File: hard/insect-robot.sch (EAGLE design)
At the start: 4 parts, among them SW1 MK-12C02, U1 ATMEGA328P-QFN32

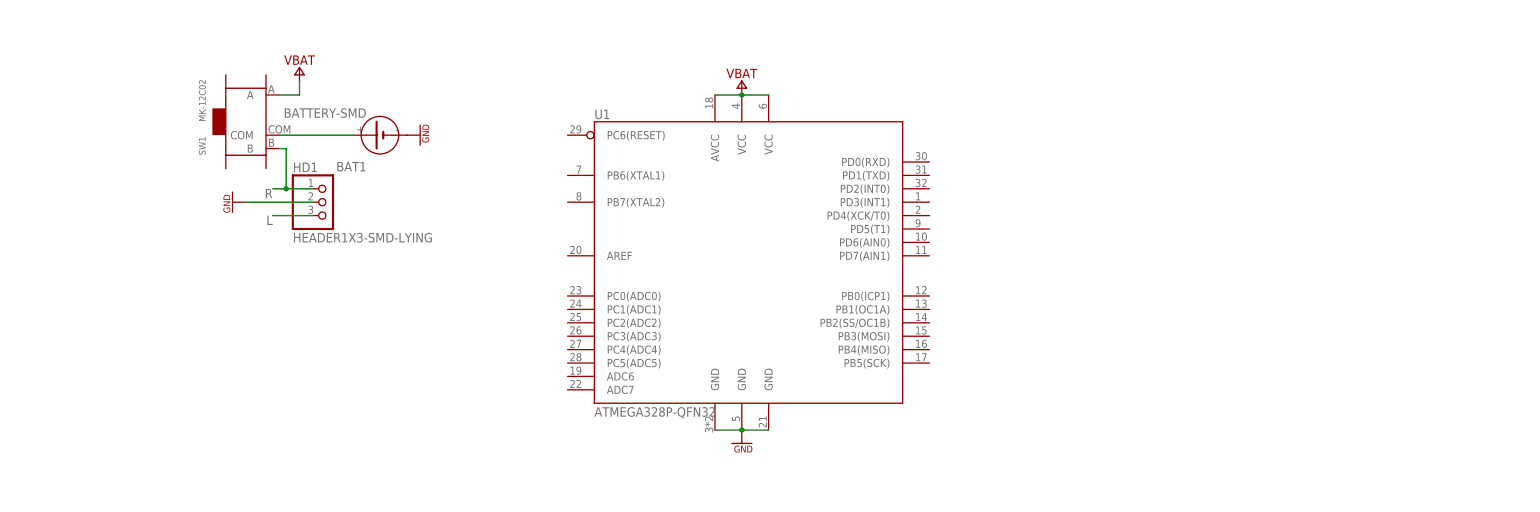
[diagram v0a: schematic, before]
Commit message: Add bluetooth module
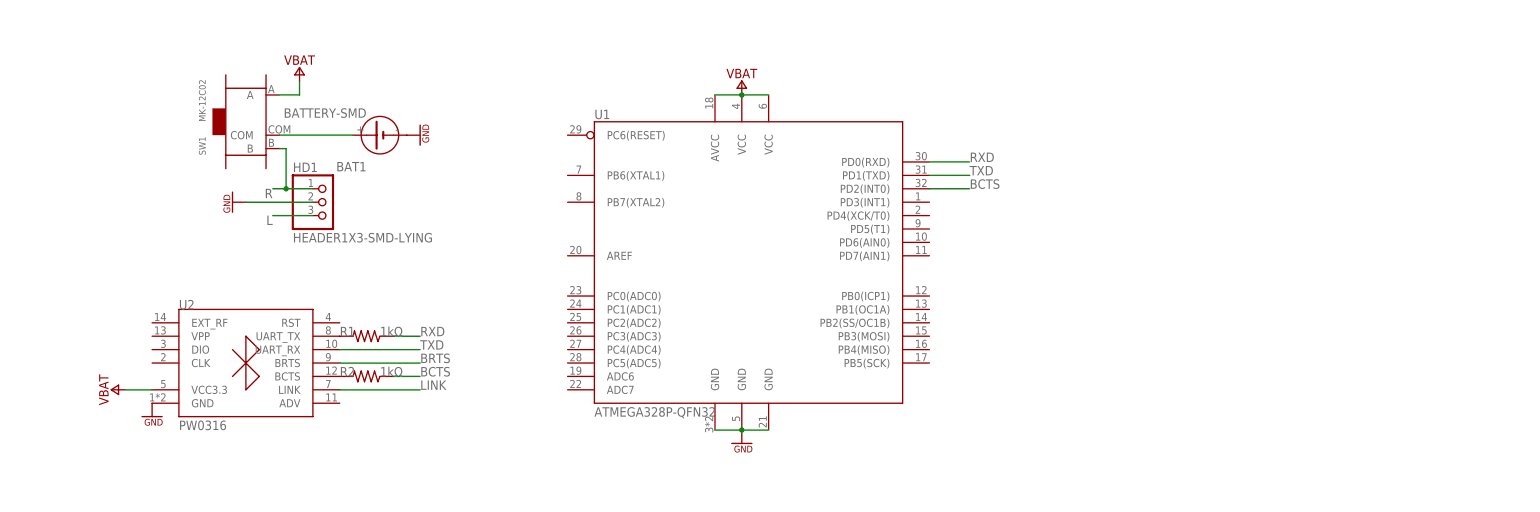
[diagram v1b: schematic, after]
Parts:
- added R1, R2: 1kΩ, MyLibrary:RES-0603
- added U2: PW0316, MyLibrary:PW0316
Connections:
- new net BCTS: R2.1, U1.PD2(INT0)
- new net BRTS: U2.BRTS
- new net LINK: U2.LINK
- new net R-BCTS: R2.2, U2.BCTS
- new net R-TX: R1.2, U2.UART_TX
- new net RXD: R1.1, U1.PD0(RXD)
- new net TXD: U1.PD1(TXD), U2.UART_RX
- net GND: now also U2.GND
- net VBAT: now also U2.VCC3.3
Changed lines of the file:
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@@
 <part name="HD1" library="MyLibrary" deviceset="HEADER1X3" device="-SMD-LYING"/>
 <part name="SUPPLY5" library="MyLibrary" deviceset="GND" device=""/>
+<part name="U2" library="MyLibrary" deviceset="PW0316" device=""/>
+<part name="SUPPLY6" library="MyLibrary" deviceset="VBAT" device=""/>
+<part name="SUPPLY7" library="MyLibrary" deviceset="GND" device=""/>
+<part name="R1" library="MyLibrary" deviceset="RES" device="-0603" value="1kΩ"/>
+<part name="R2" library="MyLibrary" deviceset="RES" device="-0603" value="1kΩ"/>
 </parts>
 <sheets>
@@
 <instance part="HD1" gate="A" x="-78.74" y="12.7"/>
 <instance part="SUPPLY5" gate="GND" x="-96.52" y="12.7" rot="R270"/>
+<instance part="U2" gate="P" x="-93.98" y="-17.78"/>
+<instance part="SUPPLY6" gate="VBAT" x="-119.38" y="-22.86" rot="R90"/>
+<instance part="SUPPLY7" gate="GND" x="-111.76" y="-27.94"/>
+<instance part="R1" gate="A" x="-71.12" y="-12.7" smashed="yes">
+<attribute name="NAME" x="-76.2" y="-12.7" size="1.778" layer="95"/>
+<attribute name="VALUE" x="-68.58" y="-12.7" size="1.778" layer="96"/>
+</instance>
+<instance part="R2" gate="A" x="-71.12" y="-20.32" smashed="yes">
+<attribute name="NAME" x="-76.2" y="-20.32" size="1.778" layer="95"/>
+<attribute name="VALUE" x="-68.58" y="-20.32" size="1.778" layer="96"/>
+</instance>
 </instances>
 <busses>
@@
 <wire x1="-83.82" y1="33.02" x2="-87.63" y2="33.02" width="0.1524" layer="91"/>
 </segment>
+<segment>
+<pinref part="U2" gate="P" pin="VCC3.3"/>
+<pinref part="SUPPLY6" gate="VBAT" pin="VBAT"/>
+<wire x1="-111.76" y1="-22.86" x2="-116.84" y2="-22.86" width="0.1524" layer="91"/>
+</segment>
 </net>
 <net name="GND" class="0">
@@
 <wire x1="-81.28" y1="12.7" x2="-93.98" y2="12.7" width="0.1524" layer="91"/>
 <pinref part="SUPPLY5" gate="GND" pin="GND"/>
+</segment>
+<segment>
+<pinref part="U2" gate="P" pin="GND"/>
+<pinref part="SUPPLY7" gate="GND" pin="GND"/>
 </segment>
 </net>
@@
 </segment>
 </net>
+<net name="RXD" class="0">
+<segment>
+<pinref part="U1" gate="P" pin="PD0(RXD)"/>
+<wire x1="35.56" y1="20.32" x2="43.18" y2="20.32" width="0.1524" layer="91"/>
+<label x="43.18" y="20.32" size="1.778" layer="95" font="vector"/>
+</segment>
+<segment>
+<pinref part="R1" gate="A" pin="1"/>
+<wire x1="-66.04" y1="-12.7" x2="-60.96" y2="-12.7" width="0.1524" layer="91"/>
+<label x="-60.96" y="-12.7" size="1.778" layer="95" font="vector"/>
+</segment>
+</net>
+<net name="TXD" class="0">
+<segment>
+<pinref part="U1" gate="P" pin="PD1(TXD)"/>
+<wire x1="35.56" y1="17.78" x2="43.18" y2="17.78" width="0.1524" layer="91"/>
+<label x="43.18" y="17.78" size="1.778" layer="95" font="vector"/>
+</segment>
+<segment>
+<pinref part="U2" gate="P" pin="UART_RX"/>
+<wire x1="-76.2" y1="-15.24" x2="-60.96" y2="-15.24" width="0.1524" layer="91"/>
+<label x="-60.96" y="-15.24" size="1.778" layer="95" font="vector"/>
+</segment>
+</net>
+<net name="BRTS" class="0">
+<segment>
+<pinref part="U2" gate="P" pin="BRTS"/>
+<wire x1="-76.2" y1="-17.78" x2="-60.96" y2="-17.78" width="0.1524" layer="91"/>
+<label x="-60.96" y="-17.78" size="1.778" layer="95" font="vector"/>
+</segment>
+</net>
+<net name="R-BCTS" class="0">
+<segment>
+<pinref part="U2" gate="P" pin="BCTS"/>
+<pinref part="R2" gate="A" pin="2"/>
+</segment>
+</net>
+<net name="BCTS" class="0">
+<segment>
+<pinref part="R2" gate="A" pin="1"/>
+<wire x1="-66.04" y1="-20.32" x2="-60.96" y2="-20.32" width="0.1524" layer="91"/>
+<label x="-60.96" y="-20.32" size="1.778" layer="95" font="vector"/>
+</segment>
+<segment>
+<pinref part="U1" gate="P" pin="PD2(INT0)"/>
+<wire x1="35.56" y1="15.24" x2="43.18" y2="15.24" width="0.1524" layer="91"/>
+<label x="43.18" y="15.24" size="1.778" layer="95" font="vector"/>
+</segment>
+</net>
+<net name="R-TX" class="0">
+<segment>
+<pinref part="U2" gate="P" pin="UART_TX"/>
+<pinref part="R1" gate="A" pin="2"/>
+</segment>
+</net>
+<net name="LINK" class="0">
+<segment>
+<pinref part="U2" gate="P" pin="LINK"/>
+<wire x1="-76.2" y1="-22.86" x2="-60.96" y2="-22.86" width="0.1524" layer="91"/>
+<label x="-60.96" y="-22.86" size="1.778" layer="95" font="vector"/>
+</segment>
+</net>

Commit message: Add MOSFET for charging control
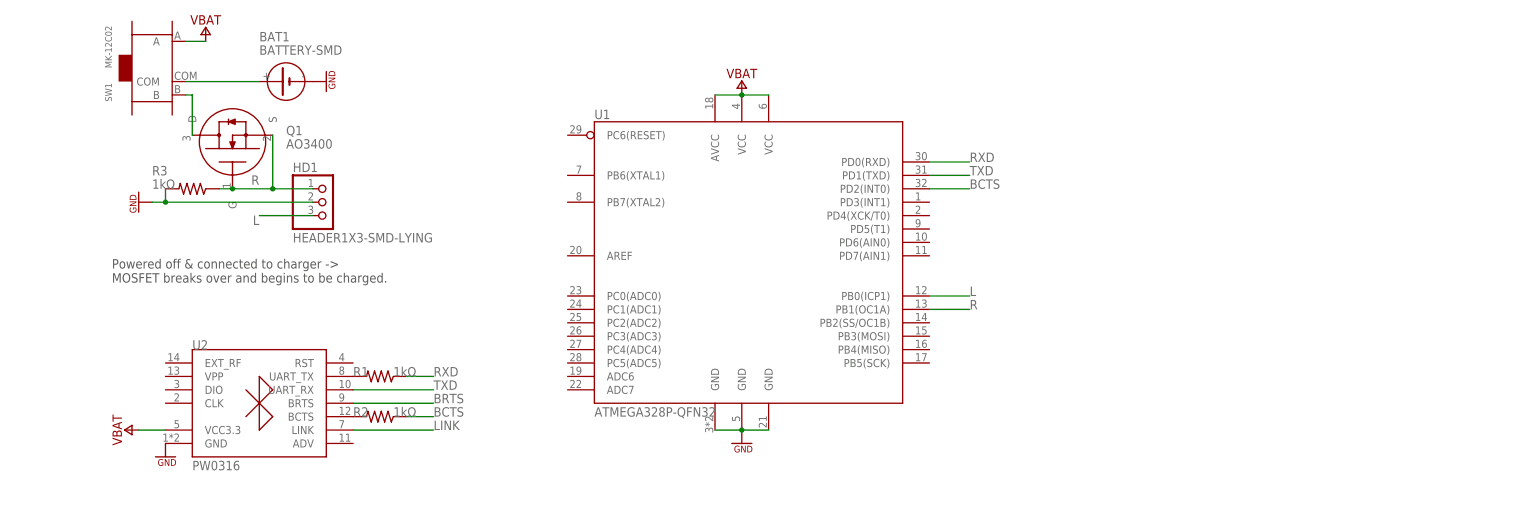
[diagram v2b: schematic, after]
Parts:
- added Q1: AO3400, MyLibrary:MOSFET-SOT23
- added R3: 1kΩ, MyLibrary:RES-0603
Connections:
- new net N$1: Q1.D, SW1.B
- net GND: now also R3.2
- net L: now also U1.PB0(ICP1)
- net R: now also Q1.G, Q1.S, R3.1, U1.PB1(OC1A); no longer SW1.B
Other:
- note added: "Powered off & connected to charger -> MOSFET breaks over and begins to be charged."
- moved on the sheet: BAT1, R1, R2, SW1, U2
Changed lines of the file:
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@@
 <part name="R1" library="MyLibrary" deviceset="RES" device="-0603" value="1kΩ"/>
 <part name="R2" library="MyLibrary" deviceset="RES" device="-0603" value="1kΩ"/>
+<part name="Q1" library="MyLibrary" deviceset="MOSFET" device="-SOT23" value="AO3400"/>
+<part name="R3" library="MyLibrary" deviceset="RES" device="-0603" value="1kΩ"/>
 </parts>
 <sheets>
 <sheet>
 <plain>
+<text x="-119.38" y="-2.54" size="1.778" layer="97">Powered off &amp; connected to charger -&gt;
+MOSFET breaks over and begins to be charged.</text>
 </plain>
 <instances>
@@
 <instance part="SUPPLY1" gate="VBAT" x="0" y="35.56"/>
 <instance part="SUPPLY2" gate="GND" x="0" y="-33.02"/>
-<instance part="SW1" gate="G$1" x="-93.98" y="27.94"/>
-<instance part="BAT1" gate="A" x="-68.58" y="25.4" rot="R180"/>
-<instance part="SUPPLY3" gate="VBAT" x="-83.82" y="38.1"/>
-<instance part="SUPPLY4" gate="GND" x="-60.96" y="25.4" rot="R90"/>
+<instance part="SW1" gate="G$1" x="-111.76" y="38.1"/>
+<instance part="BAT1" gate="A" x="-86.36" y="35.56" smashed="yes" rot="R180">
+<attribute name="NAME" x="-91.44" y="43.18" size="1.778" layer="95"/>
+<attribute name="VALUE" x="-91.44" y="40.64" size="1.778" layer="96"/>
+</instance>
+<instance part="SUPPLY3" gate="VBAT" x="-101.6" y="45.72"/>
+<instance part="SUPPLY4" gate="GND" x="-78.74" y="35.56" rot="R90"/>
 <instance part="HD1" gate="A" x="-78.74" y="12.7"/>
-<instance part="SUPPLY5" gate="GND" x="-96.52" y="12.7" rot="R270"/>
-<instance part="U2" gate="P" x="-93.98" y="-17.78"/>
-<instance part="SUPPLY6" gate="VBAT" x="-119.38" y="-22.86" rot="R90"/>
-<instance part="SUPPLY7" gate="GND" x="-111.76" y="-27.94"/>
-<instance part="R1" gate="A" x="-71.12" y="-12.7" smashed="yes">
-<attribute name="NAME" x="-76.2" y="-12.7" size="1.778" layer="95"/>
-<attribute name="VALUE" x="-68.58" y="-12.7" size="1.778" layer="96"/>
-</instance>
-<instance part="R2" gate="A" x="-71.12" y="-20.32" smashed="yes">
-<attribute name="NAME" x="-76.2" y="-20.32" size="1.778" layer="95"/>
-<attribute name="VALUE" x="-68.58" y="-20.32" size="1.778" layer="96"/>
+<instance part="SUPPLY5" gate="GND" x="-114.3" y="12.7" rot="R270"/>
+<instance part="U2" gate="P" x="-91.44" y="-25.4"/>
+<instance part="SUPPLY6" gate="VBAT" x="-116.84" y="-30.48" rot="R90"/>
+<instance part="SUPPLY7" gate="GND" x="-109.22" y="-35.56"/>
+<instance part="R1" gate="A" x="-68.58" y="-20.32" smashed="yes">
+<attribute name="NAME" x="-73.66" y="-20.32" size="1.778" layer="95"/>
+<attribute name="VALUE" x="-66.04" y="-20.32" size="1.778" layer="96"/>
+</instance>
+<instance part="R2" gate="A" x="-68.58" y="-27.94" smashed="yes">
+<attribute name="NAME" x="-73.66" y="-27.94" size="1.778" layer="95"/>
+<attribute name="VALUE" x="-66.04" y="-27.94" size="1.778" layer="96"/>
+</instance>
+<instance part="Q1" gate="A" x="-96.52" y="22.86" smashed="yes" rot="R90">
+<attribute name="NAME" x="-86.36" y="25.4" size="1.778" layer="95"/>
+<attribute name="VALUE" x="-86.36" y="22.86" size="1.778" layer="96"/>
+</instance>
+<instance part="R3" gate="A" x="-104.14" y="15.24" smashed="yes">
+<attribute name="NAME" x="-111.76" y="17.78" size="1.778" layer="95"/>
+<attribute name="VALUE" x="-111.76" y="15.24" size="1.778" layer="96"/>
 </instance>
 </instances>
@@
 </segment>
 <segment>
-<pinref part="SUPPLY3" gate="VBAT" pin="VBAT"/>
-<wire x1="-83.82" y1="35.56" x2="-83.82" y2="33.02" width="0.1524" layer="91"/>
-<pinref part="SW1" gate="G$1" pin="A"/>
-<wire x1="-83.82" y1="33.02" x2="-87.63" y2="33.02" width="0.1524" layer="91"/>
-</segment>
-<segment>
 <pinref part="U2" gate="P" pin="VCC3.3"/>
 <pinref part="SUPPLY6" gate="VBAT" pin="VBAT"/>
-<wire x1="-111.76" y1="-22.86" x2="-116.84" y2="-22.86" width="0.1524" layer="91"/>
+<wire x1="-109.22" y1="-30.48" x2="-114.3" y2="-30.48" width="0.1524" layer="91"/>
+</segment>
+<segment>
+<pinref part="SUPPLY3" gate="VBAT" pin="VBAT"/>
+<pinref part="SW1" gate="G$1" pin="A"/>
+<wire x1="-101.6" y1="43.18" x2="-105.41" y2="43.18" width="0.1524" layer="91"/>
 </segment>
 </net>
@@
 <segment>
 <pinref part="HD1" gate="A" pin="2"/>
-<wire x1="-81.28" y1="12.7" x2="-93.98" y2="12.7" width="0.1524" layer="91"/>
+<wire x1="-81.28" y1="12.7" x2="-109.22" y2="12.7" width="0.1524" layer="91"/>
 <pinref part="SUPPLY5" gate="GND" pin="GND"/>
+<pinref part="R3" gate="A" pin="2"/>
+<wire x1="-109.22" y1="12.7" x2="-111.76" y2="12.7" width="0.1524" layer="91"/>
+<wire x1="-109.22" y1="15.24" x2="-109.22" y2="12.7" width="0.1524" layer="91"/>
+<junction x="-109.22" y="12.7"/>
 </segment>
 <segment>
@@
 <pinref part="BAT1" gate="A" pin="+"/>
 <pinref part="SW1" gate="G$1" pin="COM"/>
-<wire x1="-73.66" y1="25.4" x2="-87.63" y2="25.4" width="0.1524" layer="91"/>
+<wire x1="-91.44" y1="35.56" x2="-105.41" y2="35.56" width="0.1524" layer="91"/>
 </segment>
 </net>
@@
 <segment>
 <pinref part="HD1" gate="A" pin="1"/>
-<wire x1="-81.28" y1="15.24" x2="-86.36" y2="15.24" width="0.1524" layer="91"/>
-<wire x1="-86.36" y1="15.24" x2="-86.36" y2="22.86" width="0.1524" layer="91"/>
-<pinref part="SW1" gate="G$1" pin="B"/>
-<wire x1="-86.36" y1="22.86" x2="-87.63" y2="22.86" width="0.1524" layer="91"/>
-<wire x1="-86.36" y1="15.24" x2="-88.9" y2="15.24" width="0.1524" layer="91"/>
-<junction x="-86.36" y="15.24"/>
-<label x="-88.9" y="15.24" size="1.778" layer="95" font="vector" rot="R180"/>
+<wire x1="-81.28" y1="15.24" x2="-88.9" y2="15.24" width="0.1524" layer="91"/>
+<label x="-91.44" y="17.78" size="1.778" layer="95" font="vector" rot="R180"/>
+<pinref part="Q1" gate="A" pin="G"/>
+<wire x1="-88.9" y1="15.24" x2="-96.52" y2="15.24" width="0.1524" layer="91"/>
+<pinref part="Q1" gate="A" pin="S"/>
+<wire x1="-88.9" y1="25.4" x2="-88.9" y2="15.24" width="0.1524" layer="91"/>
+<junction x="-88.9" y="15.24"/>
+<pinref part="R3" gate="A" pin="1"/>
+<wire x1="-96.52" y1="15.24" x2="-99.06" y2="15.24" width="0.1524" layer="91"/>
+<junction x="-96.52" y="15.24"/>
+</segment>
+<segment>
+<pinref part="U1" gate="P" pin="PB1(OC1A)"/>
+<wire x1="35.56" y1="-7.62" x2="43.18" y2="-7.62" width="0.1524" layer="91"/>
+<label x="43.18" y="-7.62" size="1.778" layer="95" font="vector"/>
 </segment>
 </net>
@@
 <segment>
 <pinref part="HD1" gate="A" pin="3"/>
-<wire x1="-81.28" y1="10.16" x2="-88.9" y2="10.16" width="0.1524" layer="91"/>
-<label x="-88.9" y="10.16" size="1.778" layer="95" font="vector" rot="R180"/>
+<wire x1="-81.28" y1="10.16" x2="-91.44" y2="10.16" width="0.1524" layer="91"/>
+<label x="-91.44" y="10.16" size="1.778" layer="95" font="vector" rot="R180"/>
+</segment>
+<segment>
+<pinref part="U1" gate="P" pin="PB0(ICP1)"/>
+<wire x1="35.56" y1="-5.08" x2="43.18" y2="-5.08" width="0.1524" layer="91"/>
+<label x="43.18" y="-5.08" size="1.778" layer="95" font="vector"/>
 </segment>
 </net>
@@
 <segment>
 <pinref part="R1" gate="A" pin="1"/>
-<wire x1="-66.04" y1="-12.7" x2="-60.96" y2="-12.7" width="0.1524" layer="91"/>
-<label x="-60.96" y="-12.7" size="1.778" layer="95" font="vector"/>
+<wire x1="-63.5" y1="-20.32" x2="-58.42" y2="-20.32" width="0.1524" layer="91"/>
+<label x="-58.42" y="-20.32" size="1.778" layer="95" font="vector"/>
 </segment>
 </net>
@@
 <segment>
 <pinref part="U2" gate="P" pin="UART_RX"/>
-<wire x1="-76.2" y1="-15.24" x2="-60.96" y2="-15.24" width="0.1524" layer="91"/>
-<label x="-60.96" y="-15.24" size="1.778" layer="95" font="vector"/>
+<wire x1="-73.66" y1="-22.86" x2="-58.42" y2="-22.86" width="0.1524" layer="91"/>
+<label x="-58.42" y="-22.86" size="1.778" layer="95" font="vector"/>
 </segment>
 </net>
@@
 <segment>
 <pinref part="U2" gate="P" pin="BRTS"/>
-<wire x1="-76.2" y1="-17.78" x2="-60.96" y2="-17.78" width="0.1524" layer="91"/>
-<label x="-60.96" y="-17.78" size="1.778" layer="95" font="vector"/>
+<wire x1="-73.66" y1="-25.4" x2="-58.42" y2="-25.4" width="0.1524" layer="91"/>
+<label x="-58.42" y="-25.4" size="1.778" layer="95" font="vector"/>
 </segment>
 </net>
@@
 <segment>
 <pinref part="R2" gate="A" pin="1"/>
-<wire x1="-66.04" y1="-20.32" x2="-60.96" y2="-20.32" width="0.1524" layer="91"/>
-<label x="-60.96" y="-20.32" size="1.778" layer="95" font="vector"/>
+<wire x1="-63.5" y1="-27.94" x2="-58.42" y2="-27.94" width="0.1524" layer="91"/>
+<label x="-58.42" y="-27.94" size="1.778" layer="95" font="vector"/>
 </segment>
 <segment>
@@
 <segment>
 <pinref part="U2" gate="P" pin="LINK"/>
-<wire x1="-76.2" y1="-22.86" x2="-60.96" y2="-22.86" width="0.1524" layer="91"/>
-<label x="-60.96" y="-22.86" size="1.778" layer="95" font="vector"/>
+<wire x1="-73.66" y1="-30.48" x2="-58.42" y2="-30.48" width="0.1524" layer="91"/>
+<label x="-58.42" y="-30.48" size="1.778" layer="95" font="vector"/>
+</segment>
+</net>
+<net name="N$1" class="0">
+<segment>
+<pinref part="Q1" gate="A" pin="D"/>
+<wire x1="-104.14" y1="25.4" x2="-104.14" y2="33.02" width="0.1524" layer="91"/>
+<pinref part="SW1" gate="G$1" pin="B"/>
+<wire x1="-104.14" y1="33.02" x2="-105.41" y2="33.02" width="0.1524" layer="91"/>
 </segment>
 </net>
@@
 </schematic>
 </drawing>
+<compatibility>
+<note version="6.3" minversion="6.2.2" severity="warning">
+Since Version 6.2.2 text objects can contain more than one line,
+which will not be processed correctly with this version.
+</note>
+</compatibility>
 </eagle>
